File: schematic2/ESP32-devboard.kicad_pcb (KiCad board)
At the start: 2 copper layers, 100 x 100 mm, 80 parts, among them J1 CON19x1-LEFT, J10 Screw_Terminal_01x12, J2 CON19x1-RIGHT, J3 GT-USB-7010ASV, J4 Screw_Terminal_01x10, J8 Screw_Terminal_01x16, Q1 SS8050 200-350, Q2 HL3400, Q3 SS8050 200-350, Q4 HL3400, Q5 HL3400, Q6 IRF520N, U1 ESP32-WROOM-E, U13 LTV-217-B-G, U14 LTV-217-B-G, U15 LTV-217-B-G, U16 LTV-217-B-G, U2 CP2102N-Axx-xQFN28, U3 AMS1117-3.3, U4 XL1509, U5 CD4051BM96

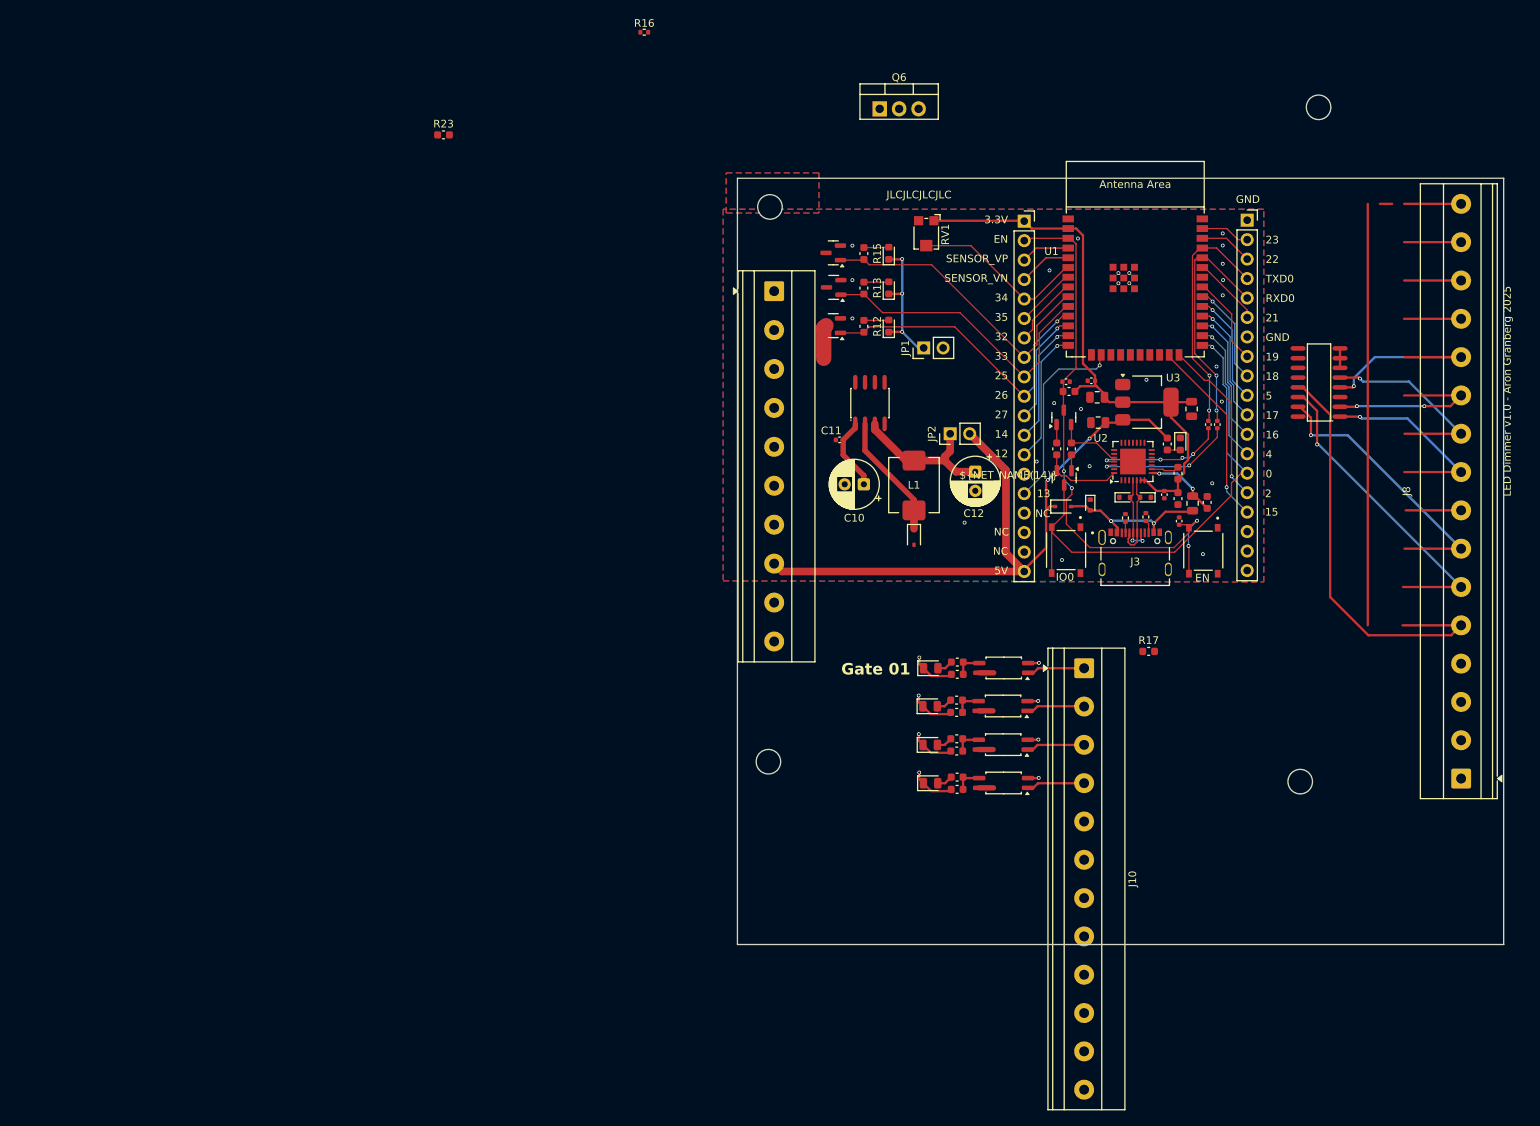
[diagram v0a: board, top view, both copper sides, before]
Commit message: Schematic updates
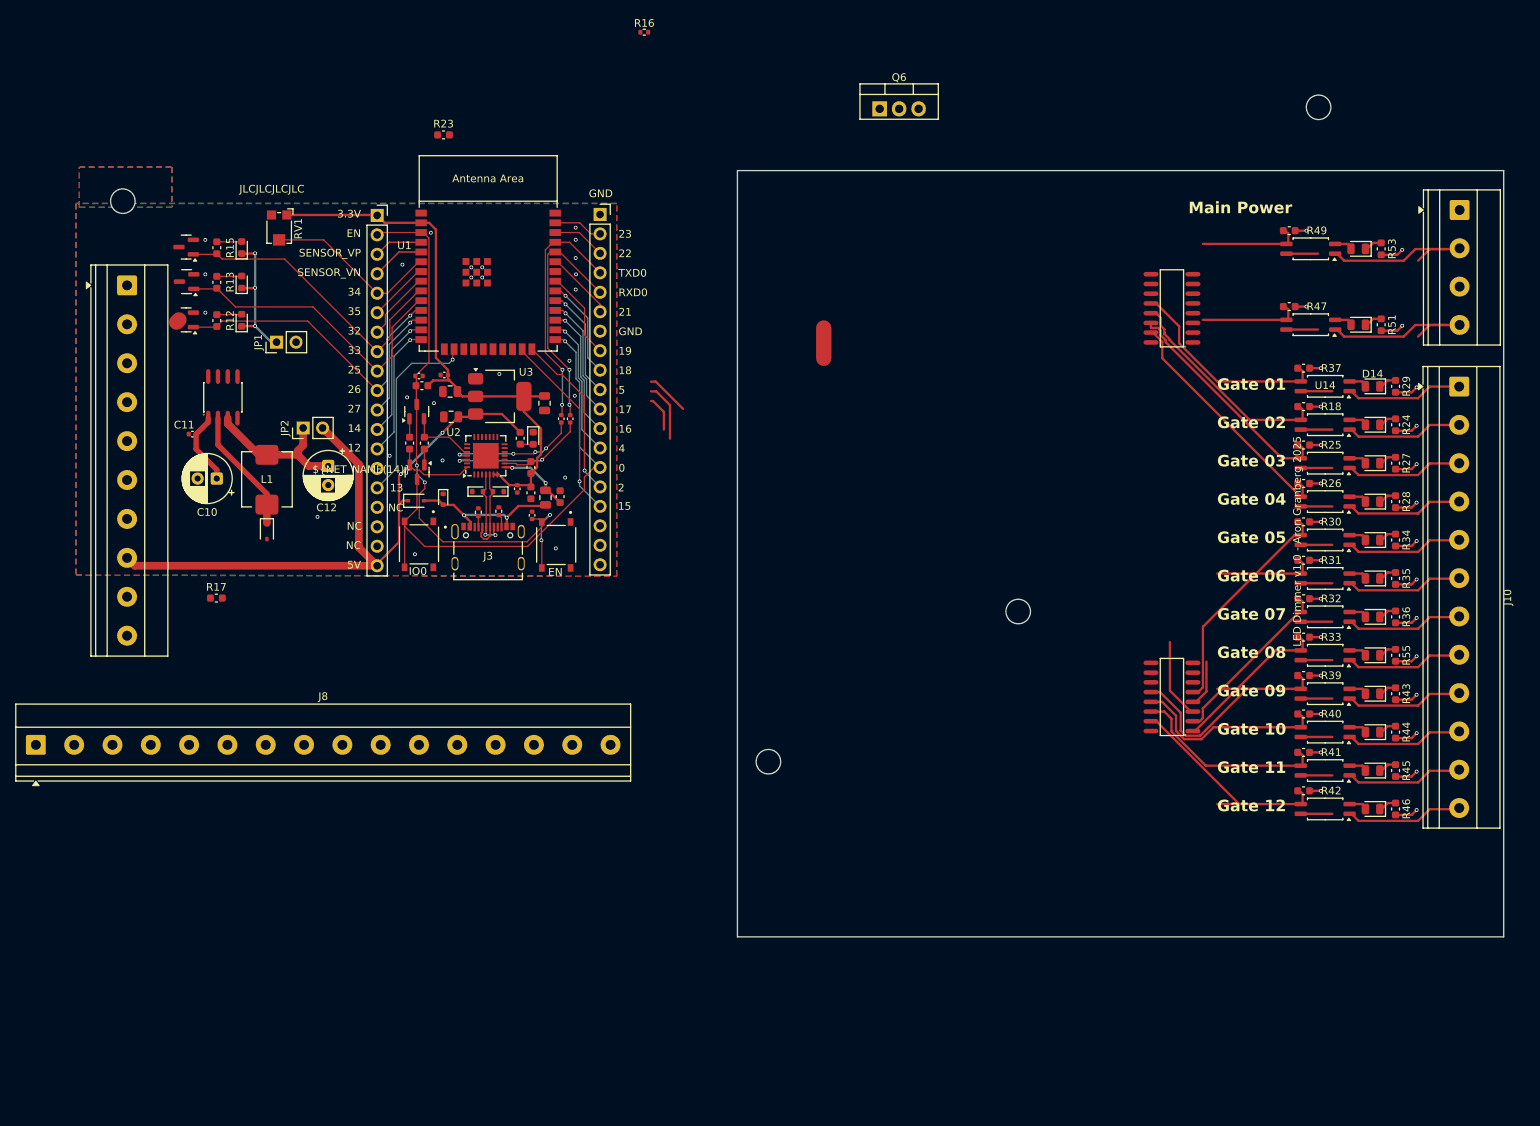
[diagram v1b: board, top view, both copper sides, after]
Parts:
- removed R38: 1k(5%), Capacitor_SMD:C_0603_1608Metric
- added D18: Green, PCM_JLCPCB:D_0805, F.Cu at (196.8, 116.7)
- added D19: Green, PCM_JLCPCB:D_0805, F.Cu at (196.8, 121.7)
- added D20: Green, PCM_JLCPCB:D_0805, F.Cu at (196.8, 126.7)
- added D21: Green, PCM_JLCPCB:D_0805, F.Cu at (196.8, 131.7)
- added D22: Green, PCM_JLCPCB:D_0805, F.Cu at (196.8, 136.7)
- added D23: Green, PCM_JLCPCB:D_0805, F.Cu at (196.8, 141.7)
- added D24: Green, PCM_JLCPCB:D_0805, F.Cu at (196.8, 146.8)
- added D25: Green, PCM_JLCPCB:D_0805, F.Cu at (196.8, 151.8)
- added D26: Green, PCM_JLCPCB:D_0805, F.Cu at (195.0, 88.6)
- added D28: Green, PCM_JLCPCB:D_0805, F.Cu at (195.0, 78.7)
- added J9: Screw_Terminal_01x04, TerminalBlock_Phoenix:TerminalBlock_Phoenix_MKDS-1,5-4_1x04_P5.00mm_Horizontal, F.Cu at (208.2, 73.6)
- added R29: 2k(5%), Capacitor_SMD:C_0603_1608Metric, F.Cu at (199.8, 96.6)
- added R30: 20K(5%), Capacitor_SMD:C_0603_1608Metric, F.Cu at (187.8, 114.3)
- added R31: 20K(5%), Capacitor_SMD:C_0603_1608Metric, F.Cu at (187.8, 119.3)
- added R32: 20K(5%), Capacitor_SMD:C_0603_1608Metric, F.Cu at (187.8, 124.3)
- added R33: 20K(5%), Capacitor_SMD:C_0603_1608Metric, F.Cu at (187.8, 129.3)
- added R34: 2k(5%), Capacitor_SMD:C_0603_1608Metric, F.Cu at (199.8, 116.7)
- added R35: 2k(5%), Capacitor_SMD:C_0603_1608Metric, F.Cu at (199.8, 121.7)
- added R36: 2k(5%), Capacitor_SMD:C_0603_1608Metric, F.Cu at (199.8, 126.7)
- added R39: 20K(5%), Capacitor_SMD:C_0603_1608Metric, F.Cu at (187.8, 134.4)
- added R40: 20K(5%), Capacitor_SMD:C_0603_1608Metric, F.Cu at (187.8, 139.4)
- added R41: 20K(5%), Capacitor_SMD:C_0603_1608Metric, F.Cu at (187.8, 144.4)
- added R42: 20K(5%), Capacitor_SMD:C_0603_1608Metric, F.Cu at (187.8, 149.4)
- added R43: 2k(5%), Capacitor_SMD:C_0603_1608Metric, F.Cu at (199.8, 136.7)
- added R44: 2k(5%), Capacitor_SMD:C_0603_1608Metric, F.Cu at (199.8, 141.7)
- added R45: 2k(5%), Capacitor_SMD:C_0603_1608Metric, F.Cu at (199.8, 146.8)
- added R46: 2k(5%), Capacitor_SMD:C_0603_1608Metric, F.Cu at (199.8, 151.8)
- added R47: 20K(5%), Capacitor_SMD:C_0603_1608Metric, F.Cu at (186.0, 86.2)
- added R49: 20K(5%), Capacitor_SMD:C_0603_1608Metric, F.Cu at (186.0, 76.3)
- added R51: 2k(5%), Capacitor_SMD:C_0603_1608Metric, F.Cu at (198.0, 88.6)
- added R53: 2k(5%), Capacitor_SMD:C_0603_1608Metric, F.Cu at (198.0, 78.7)
- added R55: 2k(5%), Capacitor_SMD:C_0603_1608Metric, F.Cu at (199.8, 131.7)
- added U17: LTV-217-B-G, PCM_JLCPCB:SOP-4_4.4x2.6mm_P1.27mm, F.Cu at (190.7, 116.7)
- added U18: LTV-217-B-G, PCM_JLCPCB:SOP-4_4.4x2.6mm_P1.27mm, F.Cu at (190.7, 121.7)
- added U19: LTV-217-B-G, PCM_JLCPCB:SOP-4_4.4x2.6mm_P1.27mm, F.Cu at (190.7, 126.7)
- added U20: LTV-217-B-G, PCM_JLCPCB:SOP-4_4.4x2.6mm_P1.27mm, F.Cu at (190.7, 131.7)
- added U21: LTV-217-B-G, PCM_JLCPCB:SOP-4_4.4x2.6mm_P1.27mm, F.Cu at (190.7, 136.7)
- added U22: LTV-217-B-G, PCM_JLCPCB:SOP-4_4.4x2.6mm_P1.27mm, F.Cu at (190.7, 141.7)
- added U23: LTV-217-B-G, PCM_JLCPCB:SOP-4_4.4x2.6mm_P1.27mm, F.Cu at (190.7, 146.8)
- added U24: LTV-217-B-G, PCM_JLCPCB:SOP-4_4.4x2.6mm_P1.27mm, F.Cu at (190.7, 151.8)
- added U25: LTV-217-B-G, PCM_JLCPCB:SOP-4_4.4x2.6mm_P1.27mm, F.Cu at (188.8, 88.6)
- added U27: LTV-217-B-G, PCM_JLCPCB:SOP-4_4.4x2.6mm_P1.27mm, F.Cu at (188.8, 78.7)
- added U29: CD4051BM96, PCM_JLCPCB:SOIC-16_L9.9-W3.9-P1.27-LS6.0-BL, F.Cu at (170.7, 86.4)
- R18, R25, R37: value 10K(5%) -> 20K(5%)
- R24, R28: value 1k(5%) -> 2k(5%)
- R26: value 1k(5%) -> 20K(5%)
- R27: value 10K(5%) -> 2k(5%)
- moved J8 186.1 mm to (22.4, 143.4), turned to 0 degrees
- moved R17 121.9 mm to (46.0, 124.2)
- moved C8 84.4 mm to (88.8, 98.8)
- moved D1 84.4 mm to (49.3, 88.0)
- moved D5 84.4 mm to (49.3, 83.0)
- moved D7 84.4 mm to (49.3, 78.5)
- moved J3 84.4 mm to (81.4, 115.0)
- moved Q3 84.4 mm to (72.1, 99.9)
- moved R12 84.4 mm to (46.0, 88.0)
- moved R13 84.4 mm to (46.0, 83.0)
- moved R14 84.4 mm to (80.1, 113.0)
- moved R15 84.4 mm to (46.0, 78.5)
- moved R7 84.4 mm to (92.1, 100.8)
- moved S2 84.4 mm to (90.3, 117.3)
- moved C1 84.4 mm to (87.0, 110.5)
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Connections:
- D14 pad 1: GND -> Net-(D14-Pad1)
- D15 pad 1: GND -> Net-(D15-Pad1)
- D16 pad 1: GND -> Net-(D16-Pad1)
- D17 pad 1: GND -> Net-(D17-Pad1)
- J10 pad 10: unconnected-(J10-Pin_10-Pad10) -> Net-(J10-Pin_10)
- J10 pad 11: unconnected-(J10-Pin_11-Pad11) -> Net-(J10-Pin_11)
- J10 pad 12: unconnected-(J10-Pin_12-Pad12) -> Net-(J10-Pin_12)
- J10 pad 5: unconnected-(J10-Pin_5-Pad5) -> Net-(J10-Pin_5)
- J10 pad 6: unconnected-(J10-Pin_6-Pad6) -> Net-(J10-Pin_6)
- J10 pad 7: unconnected-(J10-Pin_7-Pad7) -> Net-(J10-Pin_7)
- J10 pad 8: unconnected-(J10-Pin_8-Pad8) -> Net-(J10-Pin_8)
- J10 pad 9: unconnected-(J10-Pin_9-Pad9) -> Net-(J10-Pin_9)
- R18 pad 2: /Gate 1 -> /Gate 2
- R24 pad 1: Net-(D15-Pad2) -> Net-(D15-Pad1)
- R24 pad 2: /Gate 1 -> GND
- R25 pad 2: /Gate 1 -> /Gate 3
- R26 pad 1: Net-(D16-Pad2) -> GND
- R26 pad 2: /Gate 1 -> /Gate 4
- R27 pad 1: GND -> Net-(D16-Pad1)
- R27 pad 2: /Gate 1 -> GND
- R28 pad 1: Net-(D17-Pad2) -> Net-(D17-Pad1)
- R28 pad 2: /Gate 1 -> GND
- U13 pad 2: GND -> Net-(D15-Pad2)
- U13 pad 3: /Gate 1 -> /Gate 2
- U14 pad 2: GND -> Net-(D14-Pad2)
- U15 pad 2: GND -> Net-(D16-Pad2)
- U15 pad 3: /Gate 1 -> /Gate 3
- U16 pad 2: GND -> Net-(D17-Pad2)
- U16 pad 3: /Gate 1 -> /Gate 4
- U5 pad 1: /Gate 5 -> /Gate 8
- U5 pad 12: /Gate 4 -> /Gate 9
- U5 pad 13: /Gate 1 -> /Gate 10
- U5 pad 14: /Gate 2 -> /Gate 11
- U5 pad 15: /Gate 3 -> /Gate 12
- U5 pad 4: /Gate 8 -> /Gate 6
- U5 pad 5: /Gate 6 -> /Gate 5
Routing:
- net Net-(J10-Pin_1): track 8.40 -> 59.3 mm
- net /Gate 4: track 0.00 -> 31.6 mm
- net /Gate 12: track 0.00 -> 28.8 mm
- net /Gate 11: track 0.00 -> 25.3 mm
- net /Gate 10: track 0.00 -> 25.3 mm
- net GND: track 31.3 -> 55.9 mm, vias 33 -> 53
- net /Gate 6: track 25.4 -> 6.23 mm, vias 1 -> 0
- net /Gate 9: track 0.00 -> 18.8 mm
- net Net-(J10-Pin_10): track 0.00 -> 15.3 mm
- net Net-(J10-Pin_9): track 0.00 -> 15.3 mm
- net Net-(J10-Pin_6): track 0.00 -> 15.3 mm
- net Net-(J10-Pin_5): track 0.00 -> 15.3 mm
- net Net-(J10-Pin_8): track 0.00 -> 15.3 mm
- net Net-(J10-Pin_7): track 0.00 -> 15.3 mm
- net Net-(J10-Pin_12): track 0.00 -> 15.3 mm
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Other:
- board text added: "Gate 02"
- board text added: "Gate 03"
- board text added: "Gate 04"
- board text added: "Gate 05"
- board text added: "Gate 06"
- board text added: "Gate 07"
- board text added: "Gate 08"
- board text added: "Gate 09"
- board text added: "Gate 10"
- board text added: "Gate 11"
- board text added: "Gate 12"
- board text added: "Main Power"

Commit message: Schematic updates - Ordered from JLCPCB
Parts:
- removed JP1: Jumper_2_Bridged, Connector_PinHeader_2.54mm:PinHeader_1x02_P2.54mm_Vertical
- removed Q6: IRF520N, Package_TO_SOT_THT:TO-220-3_Vertical
- removed R23: 2K(5%), Capacitor_SMD:C_0603_1608Metric
- removed RV1: 10k, Potentiometer_SMD:Potentiometer_Bourns_TC33X_Vertical
- added C13: 0.1uF/50V(10%), Capacitor_SMD:C_0402_1005Metric, F.Cu at (172.2, 149.2)
- added C14: 0.1uF/50V(10%), Capacitor_SMD:C_0402_1005Metric, F.Cu at (174.2, 130.7)
- added D13: Green, PCM_JLCPCB:D_0805, F.Cu at (134.2, 112.1)
- added D27: Green, PCM_JLCPCB:D_0805, F.Cu at (197.9, 80.7)
- added D29: Green, PCM_JLCPCB:D_0805, F.Cu at (197.9, 90.7)
- added D30: Green, PCM_JLCPCB:D_0805, F.Cu at (143.5, 134.6)
- added D32: Red, PCM_JLCPCB:D_0603, F.Cu at (143.5, 139.8)
- added D33: Yellow, PCM_JLCPCB:D_0805, F.Cu at (143.5, 129.6)
- added G***: LOGO, LOGO, F.Cu at (156.2, 125.4)
- added J11: Screw_Terminal_01x03, Connector_PinHeader_2.54mm:PinHeader_1x03_P2.54mm_Horizontal, F.Cu at (194.1, 68.9)
- added J5: Screw_Terminal_01x03, Connector_PinHeader_2.54mm:PinHeader_1x03_P2.54mm_Horizontal, F.Cu at (119.0, 102.2)
- added J6: Screw_Terminal_01x03, Connector_PinHeader_2.54mm:PinHeader_1x03_P2.54mm_Horizontal, F.Cu at (119.0, 79.7)
- added J7: Screw_Terminal_01x08, TerminalBlock_Phoenix:TerminalBlock_Phoenix_MKDS-1,5-8_1x08_P5.00mm_Horizontal, F.Cu at (165.1, 160.2)
- added Q10: MMBT3904 100-300, PCM_JLCPCB:Q_SOT-23, F.Cu at (136.9, 124.3)
- added Q11: MMBT3904 100-300, PCM_JLCPCB:Q_SOT-23, F.Cu at (136.7, 134.4)
- added Q12: AO3401A, PCM_JLCPCB:Q_SOT-23, F.Cu at (130.9, 134.4)
- added Q13: MMBT3904 100-300, PCM_JLCPCB:Q_SOT-23, F.Cu at (136.8, 139.6)
- added Q14: AO3401A, PCM_JLCPCB:Q_SOT-23, F.Cu at (131.0, 139.6)
- added Q16: HL3400, PCM_JLCPCB:Q_SOT-23, F.Cu at (125.8, 91.8)
- added Q7: MMBT3904 100-300, PCM_JLCPCB:Q_SOT-23, F.Cu at (136.9, 129.3)
- added Q8: AO3401A, PCM_JLCPCB:Q_SOT-23, F.Cu at (131.1, 129.3)
- added Q9: AO3401A, PCM_JLCPCB:Q_SOT-23, F.Cu at (131.1, 124.3)
- added R19: 2K2(5%), Capacitor_SMD:C_0603_1608Metric, F.Cu at (141.5, 129.4)
- added R20: 10K(1%), Capacitor_SMD:C_0603_1608Metric, F.Cu at (134.0, 124.4)
- added R21: 2K2(5%), Capacitor_SMD:C_0603_1608Metric, F.Cu at (141.5, 124.4)
- added R22: 10K(1%), Capacitor_SMD:C_0603_1608Metric, F.Cu at (139.8, 124.4)
- added R38: 10K(1%), Capacitor_SMD:C_0603_1608Metric, F.Cu at (139.8, 129.4)
- added R48: 22K(5%), Capacitor_SMD:C_0603_1608Metric, F.Cu at (188.9, 78.3)
- added R50: 22K(5%), Capacitor_SMD:C_0603_1608Metric, F.Cu at (188.9, 88.3)
- added R52: 2K2(5%), Capacitor_SMD:C_0603_1608Metric, F.Cu at (200.9, 80.7)
- added R54: 2K2(5%), Capacitor_SMD:C_0603_1608Metric, F.Cu at (200.9, 90.7)
- added R56: 10K(1%), Capacitor_SMD:C_0603_1608Metric, F.Cu at (134.0, 129.4)
- added R57: 2K2(5%), Capacitor_SMD:C_0603_1608Metric, F.Cu at (141.3, 134.5)
- added R58: 10K(1%), Capacitor_SMD:C_0603_1608Metric, F.Cu at (139.6, 134.5)
- added R59: 10K(1%), Capacitor_SMD:C_0603_1608Metric, F.Cu at (133.8, 134.5)
- added R60: 2K2(5%), Capacitor_SMD:C_0603_1608Metric, F.Cu at (141.4, 139.7)
- added R61: 10K(1%), Capacitor_SMD:C_0603_1608Metric, F.Cu at (139.7, 139.7)
- added R62: 10K(1%), Capacitor_SMD:C_0603_1608Metric, F.Cu at (133.9, 139.7)
- added R63: 10K(1%), Capacitor_SMD:C_0603_1608Metric, F.Cu at (137.9, 119.4)
- added R64: 10K(1%), Capacitor_SMD:C_0603_1608Metric, F.Cu at (137.9, 115.8)
- added R65: 10K(1%), Capacitor_SMD:C_0603_1608Metric, F.Cu at (137.9, 111.9)
- added R68: 10K(1%), Capacitor_SMD:C_0603_1608Metric, F.Cu at (121.7, 91.8)
- added U26: LTV-217-B-G, PCM_JLCPCB:SOP-4_4.4x2.6mm_P1.27mm, F.Cu at (191.7, 80.6)
- added U28: LTV-217-B-G, PCM_JLCPCB:SOP-4_4.4x2.6mm_P1.27mm, F.Cu at (191.7, 90.7)
- D5: value Red -> Yellow; footprint PCM_JLCPCB:D_0603 -> PCM_JLCPCB:D_0805
- J1: value CON19x1-LEFT -> CON16x1-LEFT; footprint Connector_PinSocket_2.54mm:PinSocket_1x19_P2.54mm_Vertical -> Connector_PinSocket_2.54mm:PinSocket_1x16_P2.54mm_Vertical
- J2: value CON19x1-RIGHT -> CON16x1-RIGHT; footprint Connector_PinSocket_2.54mm:PinSocket_1x19_P2.54mm_Vertical -> Connector_PinSocket_2.54mm:PinSocket_1x16_P2.54mm_Vertical
- J4: value Screw_Terminal_01x10 -> Screw_Terminal_01x09; footprint TerminalBlock_Phoenix:TerminalBlock_Phoenix_MKDS-1,5-10-5.08_1x10_P5.08mm_Horizontal -> TerminalBlock_Phoenix:TerminalBlock_Phoenix_MKDS-1,5-9_1x09_P5.00mm_Horizontal
- J8: value Screw_Terminal_01x16 -> Screw_Terminal_01x03; footprint TerminalBlock_Phoenix:TerminalBlock_Phoenix_MKDS-1,5-16_1x16_P5.00mm_Horizontal -> Connector_PinHeader_2.54mm:PinHeader_1x03_P2.54mm_Horizontal
- R10, R12, R13, R15, R5: value 2K(5%) -> 2K2(5%)
- R17: value 120(1%) -> 120R(1%)
- R18, R25, R26, R30, R31, R32, R33, R37, R39, R40, R41, R42, R47, R49: value 20K(5%) -> 22K(5%)
- R24, R27, R28, R29, R34, R35, R36, R43, R44, R45, R46, R51, R53, R55: value 2k(5%) -> 2K2(5%)
- R3: footprint Capacitor_SMD:C_0805_2012Metric -> Capacitor_SMD:C_0603_1608Metric
- moved J8 110.7 mm to (119.0, 89.2), turned to 180 degrees
- moved D7 104.8 mm to (143.5, 124.4), turned to -90 degrees
- moved C11 101.5 mm to (128.5, 157.3)
- moved C10 99.1 mm to (130.6, 160.2), turned to -90 degrees
- moved JP2 99.1 mm to (141.0, 155.0), turned to 180 degrees
- moved U4 98.8 mm to (133.2, 145.9)
- moved C12 96.3 mm to (140.8, 160.2)
- moved R15 96.2 mm to (136.2, 112.0)
- moved R13 96.0 mm to (136.2, 115.8)
- moved R12 95.5 mm to (136.2, 119.4)
- moved Q5 95.2 mm to (131.1, 112.0)
- moved D8 95.0 mm to (135.7, 161.5)
- moved Q4 94.9 mm to (131.1, 115.7)
- moved Q2 94.5 mm to (131.1, 119.4)
- moved L1 93.1 mm to (134.2, 153.5), turned to 180 degrees
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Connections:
- C1 pad 2: /VDD33 -> /3.3V
- C10 pad 1: /24V_IN -> /24V
- C11 pad 1: /24V_IN -> /24V
- C2 pad 2: /VDD33 -> /3.3V
- C3 pad 1: /VDD33 -> /3.3V
- C5 pad 1: /VDD33 -> /3.3V
- C6 pad 1: /EXT_5V -> /5V
- C8 pad 1: /VDD33 -> /3.3V
- D1 pad 1: Net-(JP1-A) -> GND
- D5 pad 1: Net-(JP1-A) -> GND
- D6 pad 1: /EXT_5V -> /5V
- D7 pad 1: Net-(JP1-A) -> GND
- J1 pad 1: /VDD33 -> /3.3V
- J1 pad 15: /Dust sensor loop 2 -> /IO13
- J1 pad 16: unconnected-(J1-Pin_16-Pad16) -> /5V
- J1 pad 5: /IO34 -> /Dust sensor loop
- J4 pad 1: /24V_IN -> /Dimmer3(-)
- J4 pad 2: /LEDStrip1(-) -> /Dimmer2(-)
- J4 pad 3: /24V_IN -> /Dimmer1(-)
- J4 pad 4: /LEDStrip2(-) -> /Switch24V_R
- J4 pad 5: /24V_IN -> /Switch24V_Y
- J4 pad 6: /LEDStrip3(-) -> /Switch24V_G
- J4 pad 7: GND -> /Switch24V_Z
- J4 pad 8: GND -> /24V
- J4 pad 9: /24V_IN -> GND
- J8 pad 1: /Low pressure signal (LV) -> GND
- J8 pad 2: /Dust warning signal 1 (LV) -> /AddressableLED
- J8 pad 3: /Dust warning signal 2 (LV) -> /5V
- J9 pad 2: Net-(J9-Pin_2) -> /Low pressure signal (24V)
- J9 pad 3: Net-(J9-Pin_3) -> /High pressure signal (24V)
- JP2 pad 2: /EXT_5V -> /5V
- Q2 pad 1: /IO26 -> /IO27
- Q2 pad 3: /LEDStrip3(-) -> /Dimmer1(-)
- Q4 pad 1: /IO25 -> /IO26
- Q4 pad 3: /LEDStrip2(-) -> /Dimmer2(-)
- Q5 pad 1: /IO33 -> /IO25
- Q5 pad 3: /LEDStrip1(-) -> /Dimmer3(-)
- R10 pad 1: /EXT_5V -> /5V
- R12 pad 1: /IO26 -> /IO27
- R13 pad 1: /IO25 -> /IO26
- R15 pad 1: /IO33 -> /IO25
- R15 pad 2: Net-(D7-Pad2) -> Net-(D13-Pad2)
- R16 pad 1: /IO23 -> /IO32
- R17 pad 2: /Dust sensor loop 2 -> /Dust sensor loop
- R5 pad 1: /VDD33 -> /3.3V
- R9 pad 1: /VDD33 -> /3.3V
- U1 pad 16: /Dust sensor loop 2 -> /IO13
- U1 pad 2: /VDD33 -> /3.3V
- U1 pad 6: /IO34 -> /Dust sensor loop
- U13 pad 1: Net-(J10-Pin_2) -> Net-(J10-Pin_11)
- U14 pad 1: Net-(J10-Pin_1) -> Net-(J10-Pin_12)
- U15 pad 1: Net-(J10-Pin_3) -> Net-(J10-Pin_10)
- U16 pad 1: Net-(J10-Pin_4) -> Net-(J10-Pin_9)
- U17 pad 1: Net-(J10-Pin_5) -> Net-(J10-Pin_8)
- U18 pad 1: Net-(J10-Pin_6) -> Net-(J10-Pin_7)
- U19 pad 1: Net-(J10-Pin_7) -> Net-(J10-Pin_6)
- U2 pad 6: /VDD33 -> /3.3V
- U2 pad 7: /VDD33 -> /3.3V
- U20 pad 1: Net-(J10-Pin_8) -> Net-(J10-Pin_5)
- U21 pad 1: Net-(J10-Pin_9) -> Net-(J10-Pin_4)
- U22 pad 1: Net-(J10-Pin_10) -> Net-(J10-Pin_3)
- U23 pad 1: Net-(J10-Pin_11) -> Net-(J10-Pin_2)
- U24 pad 1: Net-(J10-Pin_12) -> Net-(J10-Pin_1)
- U25 pad 1: Net-(J9-Pin_1) -> Net-(J9-Pin_4)
- U27 pad 1: Net-(J9-Pin_3) -> /Low pressure signal (24V)
- U29 pad 10: /IO26 -> /IO18
- U29 pad 11: /IO27 -> /IO5
- U29 pad 3: /IO33 -> /IO21
- U29 pad 9: /IO25 -> /IO19
- U3 pad 2: /VDD33 -> /3.3V
- U3 pad 3: /EXT_5V -> /5V
- U4 pad 1: /24V_IN -> /24V
- U5 pad 10: /IO26 -> /IO4
- U5 pad 11: /IO27 -> /IO0
- U5 pad 3: /IO33 -> /IO17
- U5 pad 9: /IO25 -> /IO16
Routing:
- net /24V: track 0.00 -> 349.9 mm, vias 0 -> 2
- net /3.3V: track 54.2 -> 339.7 mm, vias 0 -> 2
- net /5V: track 0.00 -> 115.6 mm, vias 0 -> 3
- net /VBUS: track 20.2 -> 123.9 mm
- net /EXT_5V: track 88.5 -> 0.00 mm, vias 2 -> 0
- net /VDD33: track 75.8 -> 0.00 mm
- net /IO17: track 15.8 -> 76.8 mm
- net /IO2: track 22.0 -> 81.5 mm, vias 1 -> 2
- net /IO13: track 0.00 -> 53.6 mm, vias 0 -> 2
- net /USB-CC1: track 1.44 -> 52.6 mm
- net /USB_DP: track 10.7 -> 61.8 mm
- net /USB_DN: track 11.2 -> 62.3 mm
- net /USB-CC2: track 1.71 -> 52.9 mm
- net /Gate B2: track 0.00 -> 50.3 mm
- net /IO16: track 17.3 -> 66.6 mm
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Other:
- outline, holes or cut-outs redrawn
- board text added: "24V"
- board text added: "3.3V"
- board text added: "4-20mA"
- board text added: "5V"
- board text added: "Data"
- board text added: "Dust Collector v2.0 Aron Granberg 2026 Stockholm Makerspace"
- board text added: "Dust sensor"
- board text added: "G"
- board text added: "GND"
- board text added: "Hi"
- board text added: "LED Strip"
- board text added: "Lo"
- board text added: "P"
- board text added: "Power ON"
- board text added: "Pressure Hi"
- board text added: "Pressure Lo"
- board text added: "Pressure sensor"
- board text added: "R"
- board text added: "R2"
- board text added: "R3"
- board text added: "Temperature sensor"
- board text added: "Y"
- board text added: "Z"
- board text removed: "JLCJLCJLCJLC"
- board text removed: "LED Dimmer v1.0 - Aron Granberg 2025"
